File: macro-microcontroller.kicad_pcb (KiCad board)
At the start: 2 copper layers, 66 x 45.7 mm, 15 parts, among them J1 Conn_01x03_Pin, J2 Conn_01x02_Pin, SW1 SW_Push, SW2 SW_Push, SW3 SW_Push, U1 XIAO-RP2040-DIP

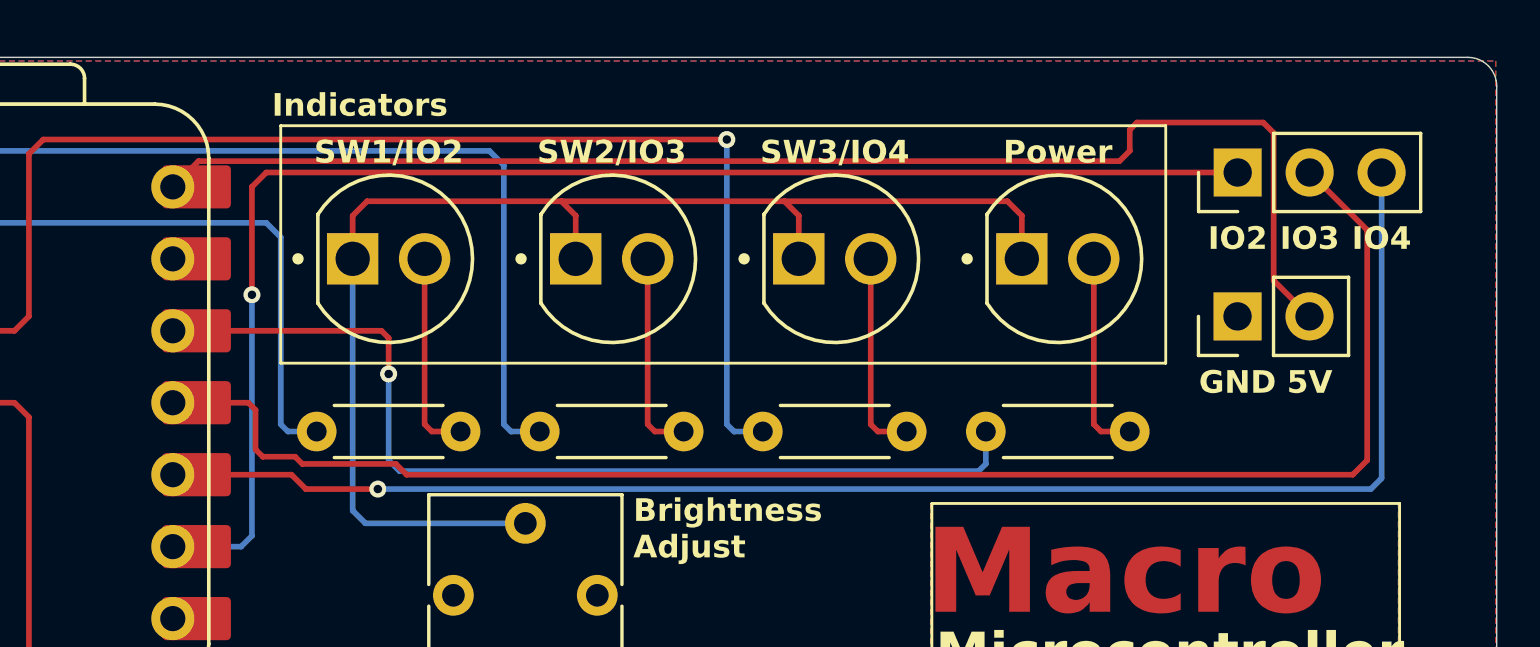
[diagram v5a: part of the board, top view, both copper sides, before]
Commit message: Reroute GPIO pins
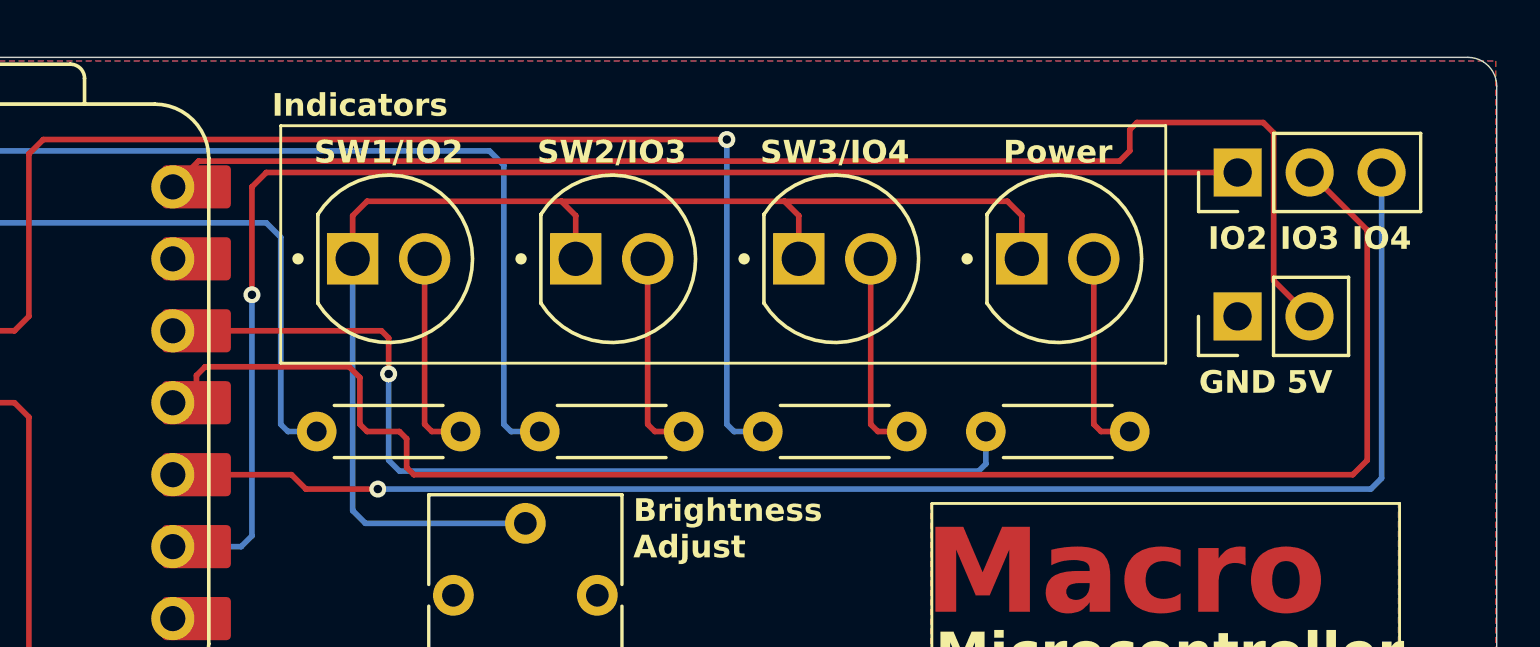
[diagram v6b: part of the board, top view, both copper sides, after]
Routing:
- net IO3: track 55.2 -> 56.8 mm
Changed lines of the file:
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@@
 	)
 	(segment
-		(start 132.334 79.883)
-		(end 129.032 79.883)
+		(start 125.603 76.454)
+		(end 130.683 76.454)
 		(width 0.2)
 		(layer "F.Cu")
@@
 	)
 	(segment
-		(start 127.381 79.375)
-		(end 127.381 77.978)
+		(start 166.624 71.628)
+		(end 164.592 69.596)
 		(width 0.2)
 		(layer "F.Cu")
@@
 	(segment
 		(start 166.116 80.264)
-		(end 132.715 80.264)
+		(end 166.624 79.756)
 		(width 0.2)
 		(layer "F.Cu")
@@
 	)
 	(segment
-		(start 164.592 69.596)
+		(start 132.969 80.264)
+		(end 166.116 80.264)
+		(width 0.2)
+		(layer "F.Cu")
+		(net 15)
+	)
+	(segment
+		(start 125.295 77.724)
+		(end 125.295 76.762)
+		(width 0.2)
+		(layer "F.Cu")
+		(net 15)
+	)
+	(segment
+		(start 132.461 78.74)
+		(end 132.715 78.994)
+		(width 0.2)
+		(layer "F.Cu")
+		(net 15)
+	)
+	(segment
+		(start 130.683 76.454)
+		(end 131.064 76.835)
+		(width 0.2)
+		(layer "F.Cu")
+		(net 15)
+	)
+	(segment
+		(start 166.624 79.756)
 		(end 166.624 71.628)
 		(width 0.2)
@@
 	)
 	(segment
-		(start 129.032 79.883)
-		(end 128.778 79.629)
+		(start 131.318 78.74)
+		(end 132.461 78.74)
 		(width 0.2)
 		(layer "F.Cu")
@@
 	)
 	(segment
-		(start 128.778 79.629)
-		(end 127.635 79.629)
+		(start 132.715 78.994)
+		(end 132.715 80.01)
 		(width 0.2)
 		(layer "F.Cu")
@@
 	)
 	(segment
-		(start 166.624 79.756)
-		(end 166.116 80.264)
+		(start 125.295 76.762)
+		(end 125.603 76.454)
 		(width 0.2)
 		(layer "F.Cu")
@@
 	)
 	(segment
-		(start 166.624 71.628)
-		(end 166.624 79.756)
+		(start 131.064 78.486)
+		(end 131.318 78.74)
 		(width 0.2)
 		(layer "F.Cu")
@@
 	)
 	(segment
-		(start 127.127 77.724)
-		(end 124.46 77.724)
+		(start 132.715 80.01)
+		(end 132.969 80.264)
 		(width 0.2)
 		(layer "F.Cu")
@@
 	)
 	(segment
-		(start 127.635 79.629)
-		(end 127.381 79.375)
+		(start 131.064 76.835)
+		(end 131.064 78.486)
 		(width 0.2)
 		(layer "F.Cu")
-		(net 15)
-	)
-	(segment
-		(start 127.381 77.978)
-		(end 127.127 77.724)
-		(width 0.2)
-		(layer "F.Cu")
-		(net 15)
-	)
-	(segment
-		(start 132.715 80.264)
-		(end 132.334 79.883)
-		(width 0.2)
-		(layer "F.Cu")
